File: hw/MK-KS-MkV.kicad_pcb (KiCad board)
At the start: 2 copper layers, 103 x 59.6 mm, 79 parts, among them J1 MuKOB IF, J2 LOOP PWR, J3 KEY-PADDLE-1_8, J4 USB-Conn, J5 RPi-GPIO40, J6 I2C Disp, J7 UART-3V3, J8 Selector-SW, Q1 MMBT3904, Q2 G01N20LE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

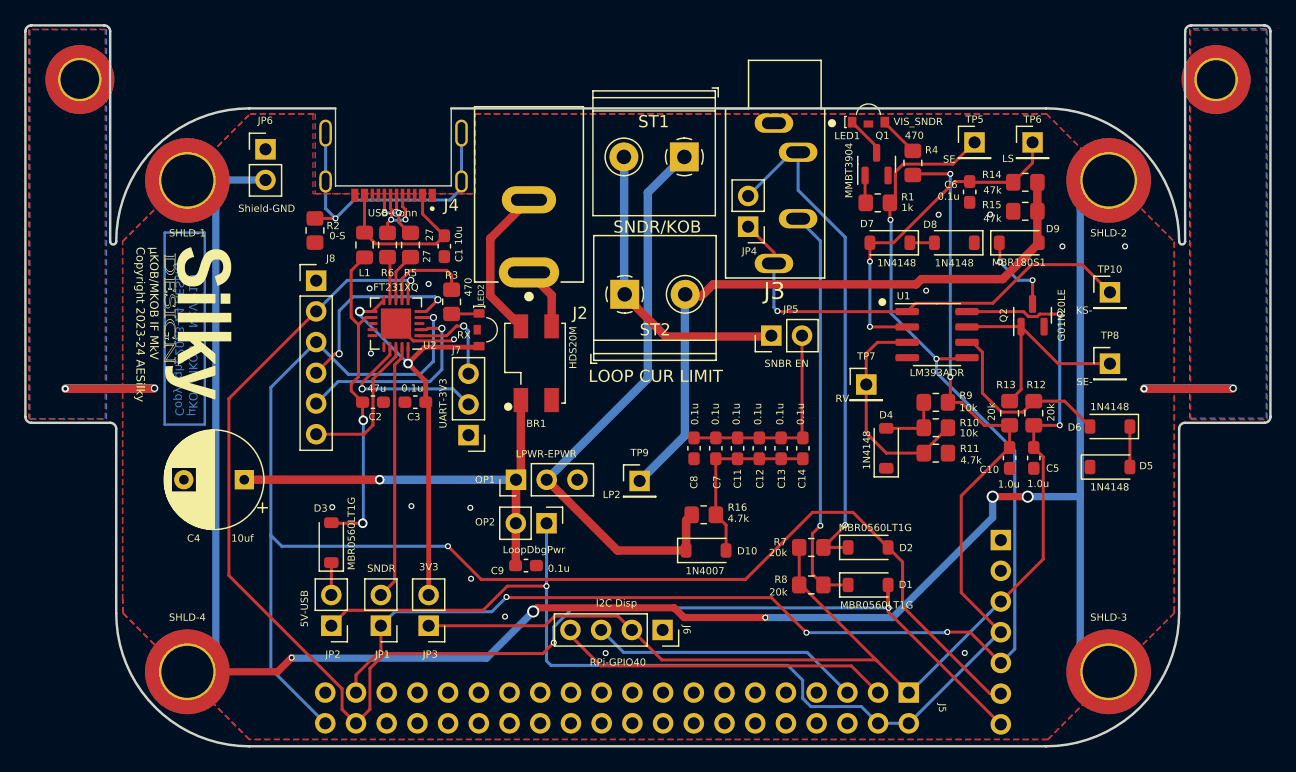
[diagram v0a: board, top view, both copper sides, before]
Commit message: Update PCB with spare and no 'ears'
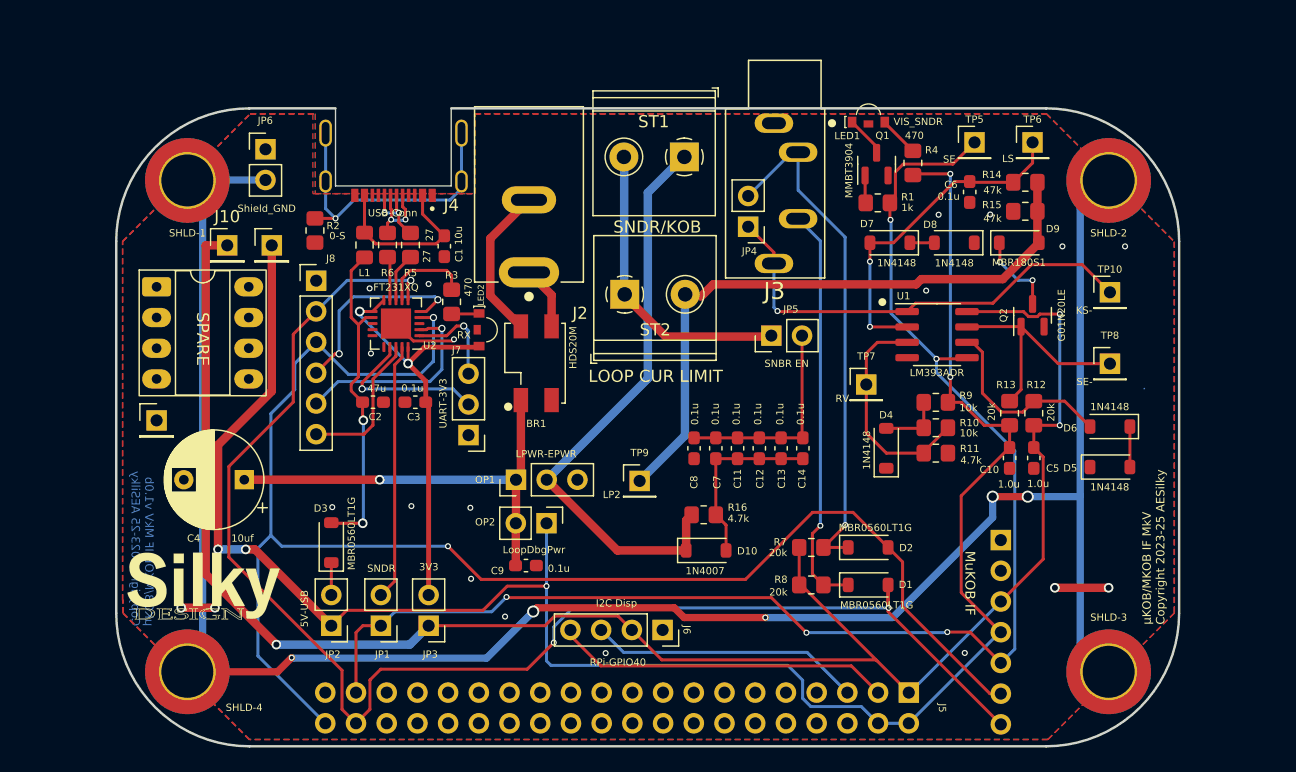
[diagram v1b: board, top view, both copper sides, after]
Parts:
- removed M_KSI1, M_KSI2: MountingHole_Pad, MountingHole:MountingHole_3.2mm_M3_ISO7380_Pad_TopBottom
- added J10: HDR 1x01 Pin, Connector_PinHeader_2.54mm:PinHeader_1x01_P2.54mm_Vertical, F.Cu at (73.4, 112.3)
- added J11: HDR 1x01 Pin, Connector_PinHeader_2.54mm:PinHeader_1x01_P2.54mm_Vertical, F.Cu at (67.6, 126.8)
- added J9: HDR 1x01 Pin, Connector_PinHeader_2.54mm:PinHeader_1x01_P2.54mm_Vertical, F.Cu at (77.1, 112.3)
- added REF**: SPARE, Package_DIP:DIP-8_W7.62mm_Socket_LongPads, F.Cu at (67.6, 115.7)
- JP6: value Shield-GND -> Shield_GND
- moved G*** 21.7 mm to (71.5, 140.5), turned to 0 degrees
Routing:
- net +3.3V: track 100.9 -> 151.4 mm, vias 2 -> 3
- net +5V: track 121.9 -> 160.9 mm, vias 3 -> 5
- net GND: track 35.0 -> 12.8 mm
- net Earth: track 173.2 -> 168.7 mm
- net /DOT-: track 123.5 -> 124.4 mm
- net /SNDR_EN: track 115.8 -> 116.7 mm
- net /DASH-: track 120.1 -> 119.5 mm
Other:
- board size 103 x 59.6 mm -> 87.9 x 52.8 mm
- board text added: "μKOB/MKOB IF MkV Copyright 2023-25 AESilky"
- board text added: "μKOB/MKOB IF MkV v1.0b Copyright 2023-25 AESilky"
- board text removed: "μKOB/MKOB IF MkV Copyright 2023-24 AESilky"
- board text removed: "μKOB/MKOB IF MkV v1.0 Copyright 2023-24 AESilky"
